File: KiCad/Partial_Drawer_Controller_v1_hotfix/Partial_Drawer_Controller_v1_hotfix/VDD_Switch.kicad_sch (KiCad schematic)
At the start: 6 parts, among them Q30 AO3400A, Q31 AO3401A

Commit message: chore: updates parts and BOM export for `Partial_Drawer_Controller_v1_hotfix`
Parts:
- R85, R86, R87: path_to_docs (none) -> Passive_Components/Resistors/UNI-ROYAL
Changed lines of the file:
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@@
 			)
 		)
-		(property "Description" ""
+		(property "Description" "Power symbol creates a global label with name \"GND\" , ground"
 			(at 171.45 67.31 0)
 			(effects
@@
 			)
 		)
-		(property "Description" ""
+		(property "Description" "Power symbol creates a global label with name \"GND\" , ground"
 			(at 135.89 104.14 0)
 			(effects
@@
 			)
 		)
-		(property "Description" ""
+		(property "Description" "Power symbol creates a global label with name \"+5V\""
 			(at 153.67 59.69 0)
 			(effects
@@
 			)
 		)
-		(property "Description" ""
+		(property "Description" "Power symbol creates a global label with name \"+5V\""
 			(at 135.89 59.69 0)
 			(effects
@@
 			)
 		)
+		(property "OC_CONRAD" ""
+			(at 135.89 71.12 0)
+			(effects
+				(font
+					(size 1.27 1.27)
+				)
+				(hide yes)
+			)
+		)
+		(property "OC_RS" ""
+			(at 135.89 71.12 0)
+			(effects
+				(font
+					(size 1.27 1.27)
+				)
+				(hide yes)
+			)
+		)
+		(property "path_to_docs" "Passive_Components/Resistors/UNI-ROYAL"
+			(at 135.89 71.12 0)
+			(effects
+				(font
+					(size 1.27 1.27)
+				)
+				(hide yes)
+			)
+		)
 		(pin "1"
 		)
@@
 			)
 		)
+		(property "OC_CONRAD" ""
+			(at 124.46 92.71 0)
+			(effects
+				(font
+					(size 1.27 1.27)
+				)
+				(hide yes)
+			)
+		)
+		(property "OC_RS" ""
+			(at 124.46 92.71 0)
+			(effects
+				(font
+					(size 1.27 1.27)
+				)
+				(hide yes)
+			)
+		)
+		(property "path_to_docs" "Passive_Components/Resistors/UNI-ROYAL"
+			(at 124.46 92.71 0)
+			(effects
+				(font
+					(size 1.27 1.27)
+				)
+				(hide yes)
+			)
+		)
 		(pin "1"
 		)
@@
 			(at 115.57 85.09 0)
 			(effects
+				(font
+					(size 1.27 1.27)
+				)
+				(hide yes)
+			)
+		)
+		(property "OC_CONRAD" ""
+			(at 115.57 85.09 0)
+			(effects
+				(font
+					(size 1.27 1.27)
+				)
+				(hide yes)
+			)
+		)
+		(property "OC_RS" ""
+			(at 115.57 85.09 0)
+			(effects
+				(font
+					(size 1.27 1.27)
+				)
+				(hide yes)
+			)
+		)
+		(property "path_to_docs" "Passive_Components/Resistors/UNI-ROYAL"
+			(at 115.57 85.09 0)
+			(effects

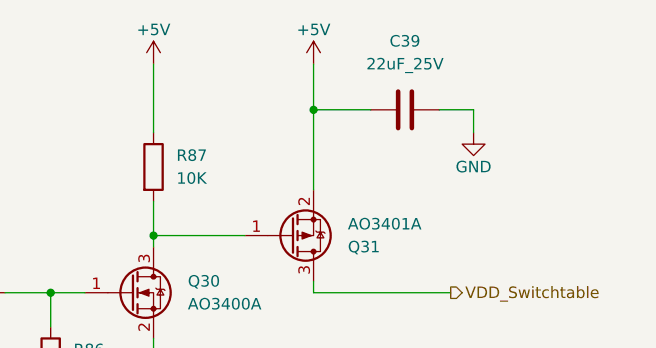
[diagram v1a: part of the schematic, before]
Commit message: chore: updates symbols for `Partial_Drawer_Controller_v1_hotfix` to get docs for every part (not finished yet)
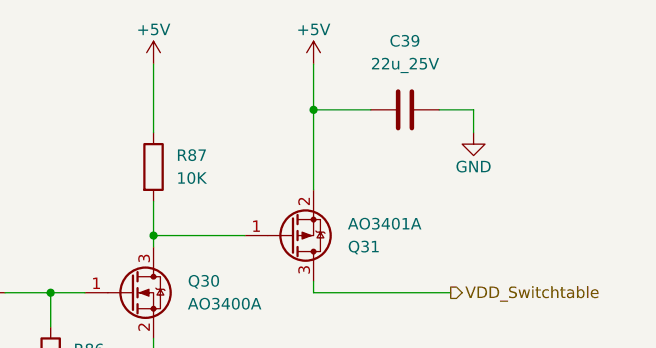
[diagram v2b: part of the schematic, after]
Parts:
- removed C39: 22uF_25V, Capacitor_SMD:C_1206_3216Metric, symbol _C_1206:22uF_25V
- added C39: 22u_25V, Capacitor_SMD:C_1206_3216Metric, symbol _C_1206:22u_25V
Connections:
- net +5V: now also C39.1
- net GND: now also C39.2

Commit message: feat: updates `Drawer_Controller_v4_hotfix` and `Partial_Drawer_Controller_v1_hotfix` with docs for MOSFETS
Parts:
- Q30, Q31: path_to_docs (none) -> Semiconductors/Discrete_Semiconductors/Transistors/MOSFETs/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
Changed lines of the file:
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@@
+			)
+		)
+		(property "OC_CONRAD" ""
+			(at 133.35 85.09 0)
+			(effects
+				(font
+					(size 1.27 1.27)
+				)
+				(hide yes)
+			)
+		)
+		(property "OC_RS" ""
+			(at 133.35 85.09 0)
+			(effects
+				(font
+					(size 1.27 1.27)
+				)
+				(hide yes)
+			)
+		)
+		(property "path_to_docs" "Semiconductors/Discrete_Semiconductors/Transistors/MOSFETs/AO3400A"
+			(at 133.35 85.09 0)
+			(effects
+				(font
+					(size 1.27 1.27)
+				)
+				(hide yes)
 			)
 		)
@@
 			(at 151.13 78.74 0)
 			(effects
+				(font
+					(size 1.27 1.27)
+				)
+				(hide yes)
+			)
+		)
+		(property "OC_CONRAD" ""
+			(at 151.13 78.74 0)
+			(effects
+				(font
+					(size 1.27 1.27)
+				)
+				(hide yes)
+			)
+		)
+		(property "OC_RS" ""
+			(at 151.13 78.74 0)
+			(effects
+				(font
+					(size 1.27 1.27)
+				)
+				(hide yes)
+			)
+		)
+		(property "path_to_docs" "Semiconductors/Discrete_Semiconductors/Transistors/MOSFETs/AO3401A"
+			(at 151.13 78.74 0)
+			(effects
